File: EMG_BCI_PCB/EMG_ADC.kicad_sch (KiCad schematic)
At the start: 6 parts, among them U5 ADS1013IDGS

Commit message: More schematic changes
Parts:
- removed R18, R19, R20: 10K, Resistor_SMD:R_0805_2012Metric_Pad1.15x1.40mm_HandSolder, symbol Device:R
- removed U5: ADS1013IDGS, Package_SO:TSSOP-10_3x3mm_P0.5mm, symbol Analog_ADC:ADS1013IDGS
- added U9: MCP3202, symbol Analog_ADC:MCP3202
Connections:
- net +5V: now also U9.8 (VDD/VREF)
- net Earth: now also U9.4 (VSS)
- new net AdcCh0: U9.2 (CH0)
- new net AdcCh1: U9.3 (CH1)
- new net CLK: U9.7 (CLK)
- new net DIN: U9.5 (DIN)
- new net DOUT: U9.6 (DOUT)
- new net ~{CS}/SHDN: U9.1 (~{CS}/SHDN)
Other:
- moved on the sheet: C23, C24

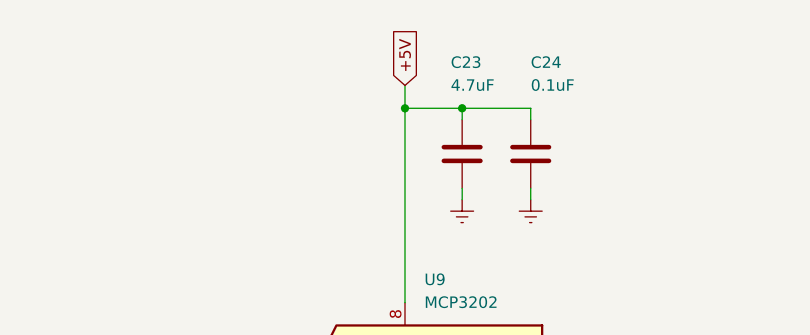
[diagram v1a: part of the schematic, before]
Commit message: Added power symbols for +/-3.3V
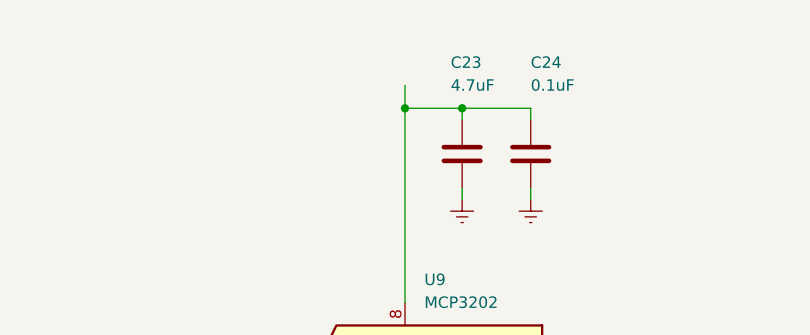
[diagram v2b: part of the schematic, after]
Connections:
- net +5V: no longer names the net of C23.1, C24.1, U9.8 (VDD/VREF)
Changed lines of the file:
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@@
-		)
-	)
-	(global_label "+5V"
-		(shape input)
-		(at 149.86 69.85 90)
-		(effects
-			(font
-				(size 1.27 1.27)
-			)
-			(justify left)
-		)
-		(property "Intersheetrefs" "${INTERSHEET_REFS}"
-			(at 149.86 69.85 0)
-			(effects
-				(font
-					(size 1.27 1.27)
-				)
-				(hide yes)
-			)
 		)
 	)

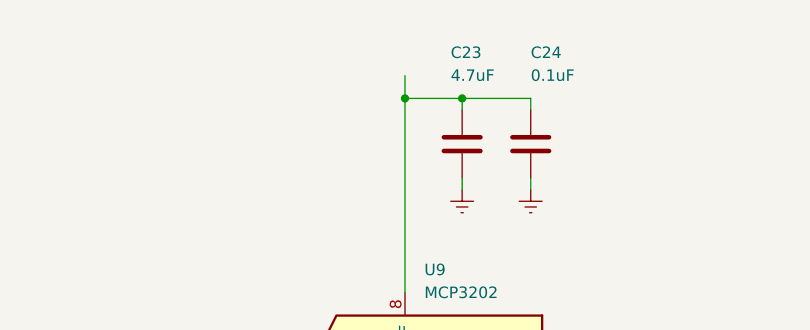
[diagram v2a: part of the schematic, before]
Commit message: Removed some warnings from the electrical rules
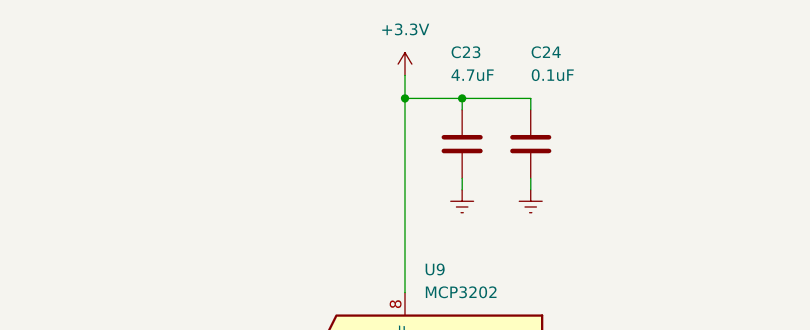
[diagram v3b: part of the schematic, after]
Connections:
- net +3.3V: now reaches C23.1, C24.1, U9.8 (VDD/VREF)
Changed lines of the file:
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@@
+	)
+	(symbol
+		(lib_id "power:+3.3V")
+		(at 149.86 69.85 0)
+		(unit 1)
+		(exclude_from_sim no)
+		(in_bom yes)
+		(on_board yes)
+		(dnp no)
+		(fields_autoplaced yes)
+		(property "Reference" "#PWR043"
+			(at 149.86 73.66 0)
+			(effects
+				(font
+					(size 1.27 1.27)
+				)
+				(hide yes)
+			)
+		)
+		(property "Value" "+3.3V"
+			(at 149.86 64.77 0)
+			(effects
+				(font
+					(size 1.27 1.27)
+				)
+			)
+		)
+		(property "Footprint" ""
+			(at 149.86 69.85 0)
+			(effects
+				(font
+					(size 1.27 1.27)
+				)
+				(hide yes)
+			)
+		)
+		(property "Datasheet" ""
+			(at 149.86 69.85 0)
+			(effects
+				(font
+					(size 1.27 1.27)
+				)
+				(hide yes)
+			)
+		)
+		(property "Description" "Power symbol creates a global label with name \"+3.3V\""
+			(at 149.86 69.85 0)
+			(effects
+				(font
+					(size 1.27 1.27)
+				)
+				(hide yes)
+			)
+		)
+		(pin "1"
+		)
+		(instances
+			(project "EMG_BCI_PCB"
+				(path "/55cf2478-b5ba-45ce-afa6-3f75a1bb5fb4/00000000-0000-0000-0000-00005f1208c1"
+					(reference "#PWR043")
+					(unit 1)
+				)
+			)
+		)
 	)
 	(symbol

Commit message: Assigned footprints to components
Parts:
- C23, C24: footprint Capacitor_SMD:C_0603_1608Metric_Pad1.05x0.95mm_HandSolder -> Capacitor_SMD:C_0201_0603Metric_Pad0.64x0.40mm_HandSolder
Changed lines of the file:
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@@
 			)
 		)
-		(property "Footprint" "Capacitor_SMD:C_0603_1608Metric_Pad1.05x0.95mm_HandSolder"
+		(property "Footprint" "Capacitor_SMD:C_0201_0603Metric_Pad0.64x0.40mm_HandSolder"
 			(at 157.1752 81.28 0)
 			(effects
@@
 			)
 		)
-		(property "Footprint" "Capacitor_SMD:C_0603_1608Metric_Pad1.05x0.95mm_HandSolder"
+		(property "Footprint" "Capacitor_SMD:C_0201_0603Metric_Pad0.64x0.40mm_HandSolder"
 			(at 164.7952 81.28 0)
 			(effects

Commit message: finally assigned the footprints to the schematic symbols
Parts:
- U9: footprint (none) -> Wills_FootprintLibrary:8-MSOP
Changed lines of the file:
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@@
 			)
 		)
-		(property "Footprint" ""
+		(property "Footprint" "Wills_FootprintLibrary:8-MSOP"
 			(at 149.86 109.22 0)
 			(effects

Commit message: Initial placement and routing
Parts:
- C23, C24: footprint Capacitor_SMD:C_0201_0603Metric_Pad0.64x0.40mm_HandSolder -> Capacitor_SMD:C_0603_1608Metric_Pad1.08x0.95mm_HandSolder
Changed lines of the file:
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@@
 			)
 		)
-		(property "Footprint" "Capacitor_SMD:C_0201_0603Metric_Pad0.64x0.40mm_HandSolder"
+		(property "Footprint" "Capacitor_SMD:C_0603_1608Metric_Pad1.08x0.95mm_HandSolder"
 			(at 157.1752 81.28 0)
 			(effects
@@
 			)
 		)
-		(property "Footprint" "Capacitor_SMD:C_0201_0603Metric_Pad0.64x0.40mm_HandSolder"
+		(property "Footprint" "Capacitor_SMD:C_0603_1608Metric_Pad1.08x0.95mm_HandSolder"
 			(at 164.7952 81.28 0)
 			(effects
